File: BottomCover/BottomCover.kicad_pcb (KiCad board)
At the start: 2 copper layers, 134.8 x 98.3 mm, 6 parts

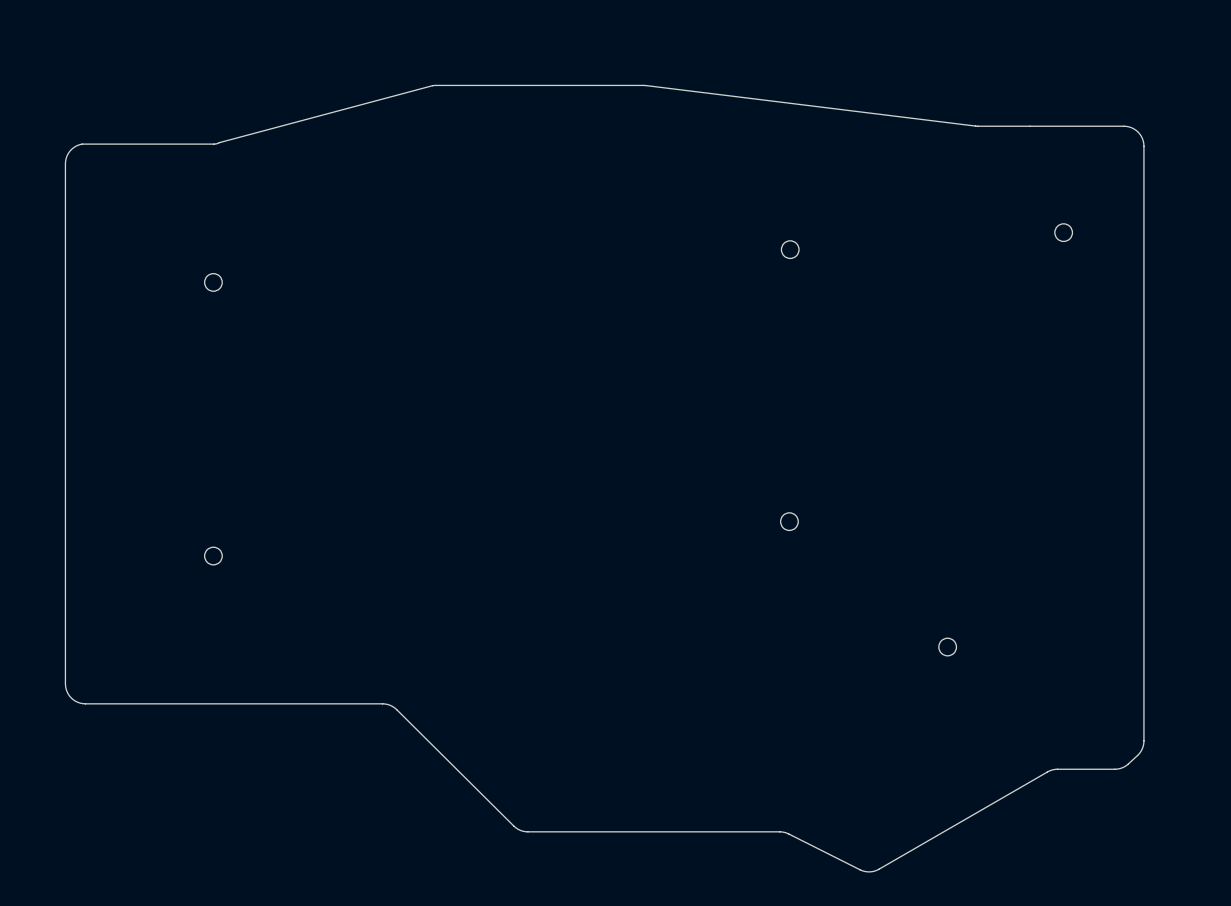
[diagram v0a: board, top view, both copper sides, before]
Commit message: minor updates for SMD assembly
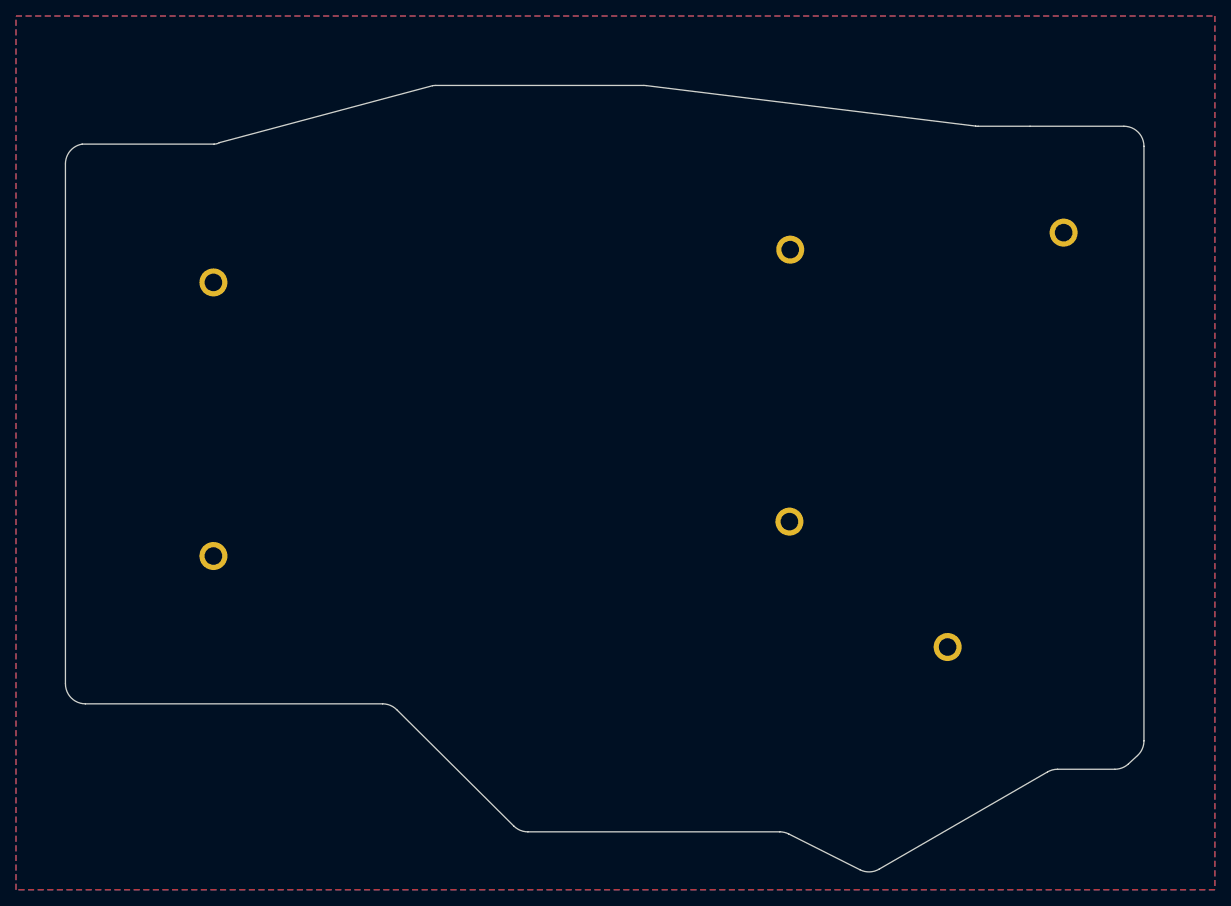
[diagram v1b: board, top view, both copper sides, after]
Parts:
- H1, H2, H3, H4, H5, H6: footprint MountingHole:MountingHole_2.2mm_M2 -> MountingHole:MountingHole_2.2mm_M2_ISO7380_Pad
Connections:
- H1 pad 1: unconnected-(H1-Pad1) -> GND
- H2 pad 1: unconnected-(H2-Pad1) -> GND
- H3 pad 1: unconnected-(H3-Pad1) -> GND
- H4 pad 1: unconnected-(H4-Pad1) -> GND
- H5 pad 1: unconnected-(H5-Pad1) -> GND
- H6 pad 1: unconnected-(H6-Pad1) -> GND
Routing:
- added copper zone on B.Cu, net GND
- added copper zone on F.Cu, net GND
